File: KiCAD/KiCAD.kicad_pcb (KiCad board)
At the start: 2 copper layers, 200 x 150 mm, 199 parts, among them J1 Conn_01x02_Pin, J11 GRID_BIAS, J12 CATHODE_SENSE, J13 Conn_01x05, J14 Conn_01x02_Pin, J15 Conn_01x03_Pin, J16 Conn_01x05, J3 Conn_01x02_Pin, J4 8P8C_Shielded, J5 ENC_INT if needed, J6 TX/RX, J7 HV, J8 HV_INRUSH_BYPASS, J9 TR_SENSE, Q1 J310, Q2 2N7000, Q3 2N7000, Q4 2N7000, Q5 2N7000, Q6 2N7000, Q7 2N7000, T1 2N3906, T2 2N3906, U1 Si5351A_Breakout, U10 OPA454, U11 LM4040LP-5, U12 LM393, U13 OPA1641, U14 OPA1641, U15 LM7805_TO220, U16 AM26LS32ACN, U17 Adafruit_PCF8575_Breakout, U18 CD14538B, U19 L79L08_TO92, U20 ICL7660S, U3 MC1496, U4 MCP4921, U5 OPA454, U6 LM7171xIN, U7 LM7171xIN, U8 MCP4728, U9 LM7805_TO220

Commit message: kicad: L79L08 local decoupling; unlink bias sheet from root
- Add C17/C18 (0.33 uF Z5U SR205E334MAR) at L79L08 in/out to prevent
  oscillation and damp L7+U19 ringing
- New footprint xmitter:Kyocera_SR20_MLCC for the SR20 style radial MLCC
  (2.54 mm pitch, 5.08 x 3.175 mm body)
- Add SR-Series datasheet to Documentation/Components
- Unlink bias sheet from root schematic — first step in splitting the
  bias circuit onto its own PCB

Co-Authored-By: Claude Opus 4.7 <noreply@anthropic.com>
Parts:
- removed C19, C20, C23, C24, C27, C31: 100nF, Capacitor_THT:C_Disc_D5.0mm_W2.5mm_P5.00mm
- removed C21: 0.33uF, Capacitor_THT:C_Rect_L7.0mm_W3.5mm_P5.00mm
- removed C22: 0.1uF, Capacitor_THT:C_Disc_D5.0mm_W2.5mm_P5.00mm
- removed C25, C26, C30, C32, C33: 10uF, Capacitor_THT:CP_Radial_D5.0mm_P2.00mm
- removed C28, C29: 1nF, Capacitor_THT:C_Rect_L7.0mm_W3.5mm_P5.00mm
- removed D1, D2, D3, D4: 1N5817, Diode_THT:D_DO-41_SOD81_P10.16mm_Horizontal
- removed D5, D6: 1N4148, Diode_THT:D_DO-35_SOD27_P7.62mm_Horizontal
- removed J11: GRID_BIAS, Connector_PinHeader_2.54mm:PinHeader_1x02_P2.54mm_Vertical
- removed J12: CATHODE_SENSE, Connector_PinHeader_2.54mm:PinHeader_1x02_P2.54mm_Vertical
- removed J14, J3 (x2): Conn_01x02_Pin, Connector_PinHeader_2.54mm:PinHeader_1x02_P2.54mm_Vertical
- removed Q2, Q3: 2N7000, Package_TO_SOT_THT:TO-92_Inline
- removed R17: 27K, Resistor_THT:R_Axial_DIN0207_L6.3mm_D2.5mm_P10.16mm_Horizontal
- removed R18, R_GA1, R_GATE1, R_GB1: 10K, Resistor_THT:R_Axial_DIN0207_L6.3mm_D2.5mm_P10.16mm_Horizontal
- removed R19, R25: 4.7K, Resistor_THT:R_Axial_DIN0207_L6.3mm_D2.5mm_P10.16mm_Horizontal
- removed R20, R22: 7.5K, Resistor_THT:R_Axial_DIN0207_L6.3mm_D2.5mm_P10.16mm_Horizontal
- removed R21, R23: 470K, Resistor_THT:R_Axial_DIN0207_L6.3mm_D2.5mm_P10.16mm_Horizontal
- removed R24: 100K, Resistor_THT:R_Axial_DIN0207_L6.3mm_D2.5mm_P10.16mm_Horizontal
- removed RV1: 10K, Potentiometer_THT:Potentiometer_Bourns_3296W_Vertical
- removed R_FA1, R_FB1: 170K, Resistor_THT:R_Axial_DIN0207_L6.3mm_D2.5mm_P10.16mm_Horizontal
- removed R_GLA1, R_GLB1: 22K, Resistor_THT:R_Axial_DIN0207_L6.3mm_D2.5mm_P10.16mm_Horizontal
- removed R_PADA1, R_PADB1: 1K, Resistor_THT:R_Axial_DIN0207_L6.3mm_D2.5mm_P10.16mm_Horizontal
- removed R_Z1: 2.2K, Resistor_THT:R_Axial_DIN0207_L6.3mm_D2.5mm_P10.16mm_Horizontal
- removed TP10: CRASH_A, Connector_PinHeader_2.54mm:PinHeader_1x01_P2.54mm_Vertical
- removed TP8: GRID_CRASH, Connector_PinHeader_2.54mm:PinHeader_1x01_P2.54mm_Vertical
- removed TP9: CRASH_B, Connector_PinHeader_2.54mm:PinHeader_1x01_P2.54mm_Vertical
- removed U10, U5: OPA454, Package_DIP:DIP-8_W7.62mm
- removed U11: LM4040LP-5, Package_TO_SOT_THT:TO-92_Inline
- removed U12: LM393, Package_DIP:DIP-8_W7.62mm
- removed U13, U14: OPA1641, Package_DIP:DIP-8_W7.62mm
- removed U9: LM7805_TO220, Package_TO_SOT_THT:TO-220-3_Vertical
- C17, C18: value 1uF -> 0.33uF; footprint Capacitor_THT:C_Rect_L7.2mm_W4.5mm_P5.00mm -> xmitter:Kyocera_SR20_MLCC
- moved C17 259.5 mm to (93.8, 52.5)
- moved C18 255.0 mm to (87.8, 46.0)
- moved C48 21.8 mm to (99.5, 38.5)
- moved TP20 15.9 mm to (74.0, 42.0)
- moved J15 6.60 mm to (120.0, 158.5), turned to 180 degrees
- moved C43 3.53 mm to (95.5, 128.5)
- moved U19 3.35 mm to (95.0, 46.5)
- moved J6 2.54 mm to (120.5, 102.0)
- moved J7 2.54 mm to (120.5, 110.0)
- moved J8 2.54 mm to (120.5, 118.0)
- moved C42 2.50 mm to (96.0, 117.5)
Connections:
- C17 pad 1: +5V -> VEE
- C18 pad 1: GND -> Net-(U19-VI)
- C18 pad 2: -90V -> GND

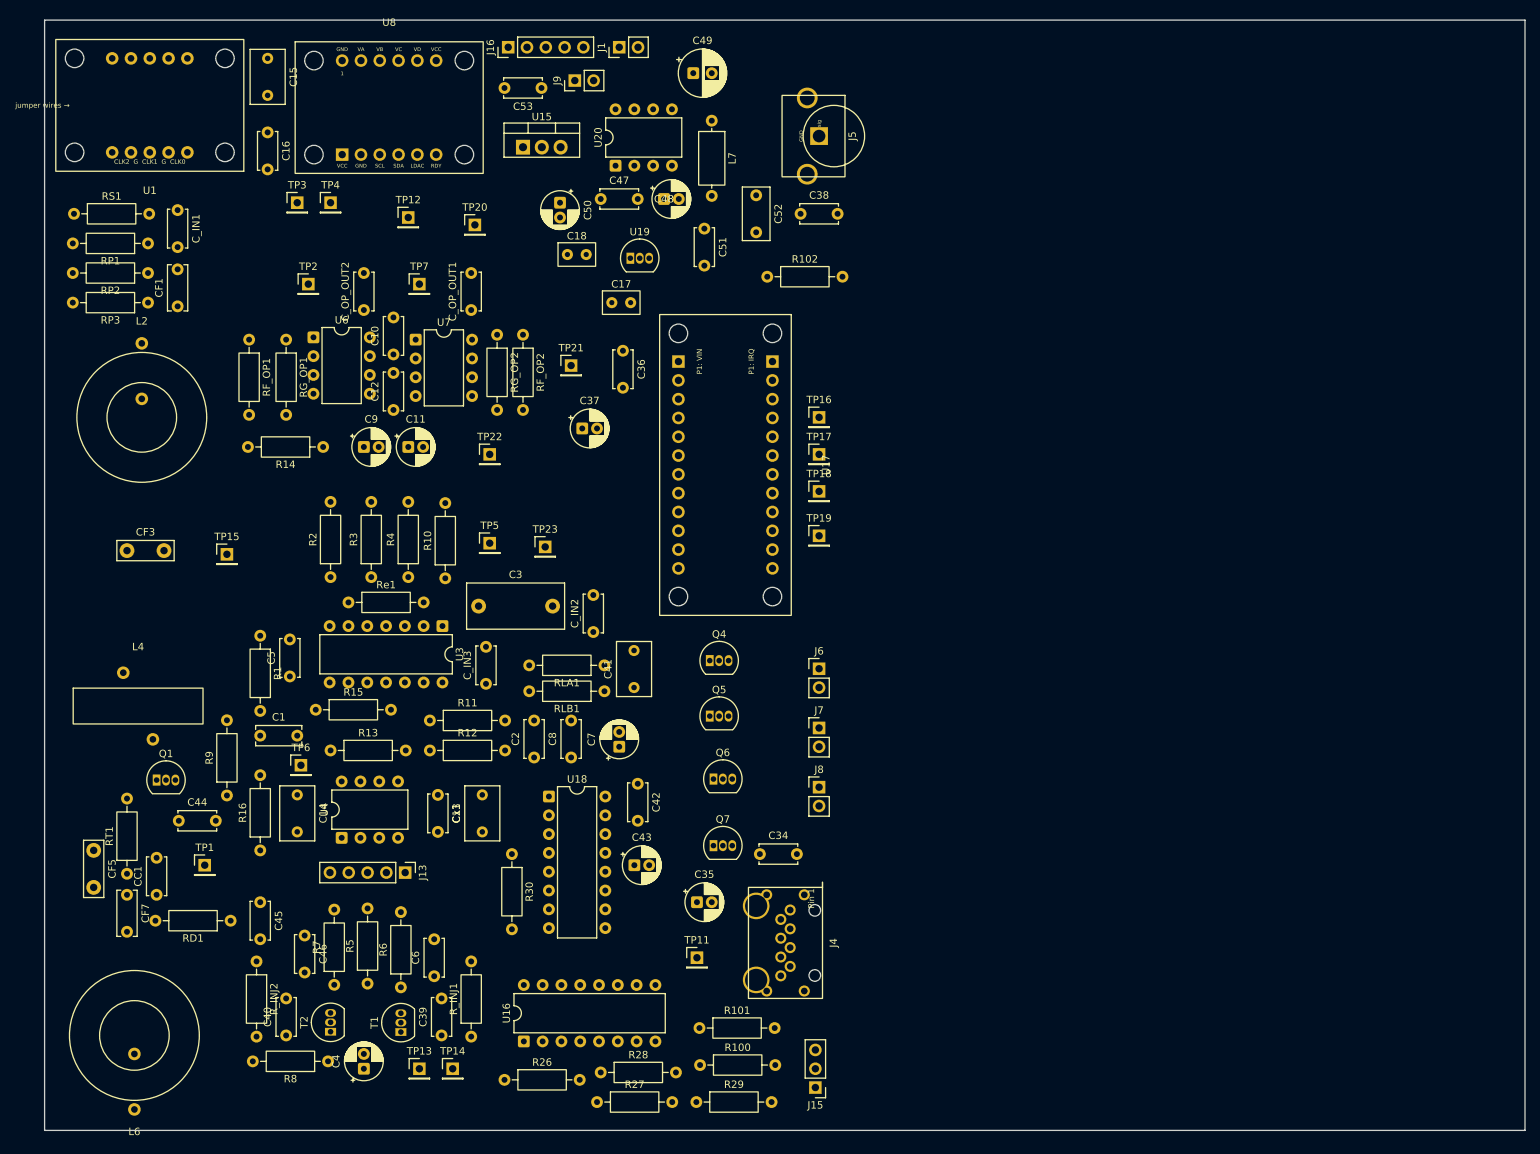
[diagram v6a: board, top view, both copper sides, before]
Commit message: kicad: net classes for Power/RF/HIZ with patterns for labeled nets
Adds Power (0.5mm/0.2mm), RF (0.4mm/0.25mm), and HIZ (0.3mm/0.25mm)
classes with color-coding. Patterns catch +12V/+5V/3V3/VEE/GND and
RAW_RF/MOD_RF_OUT+/- automatically. Anonymous nets (MC1496 out, DAC
output, T1/T2 collectors, injection paths) still need labels or
manual assignment.

Co-Authored-By: Claude Opus 4.7 <noreply@anthropic.com>
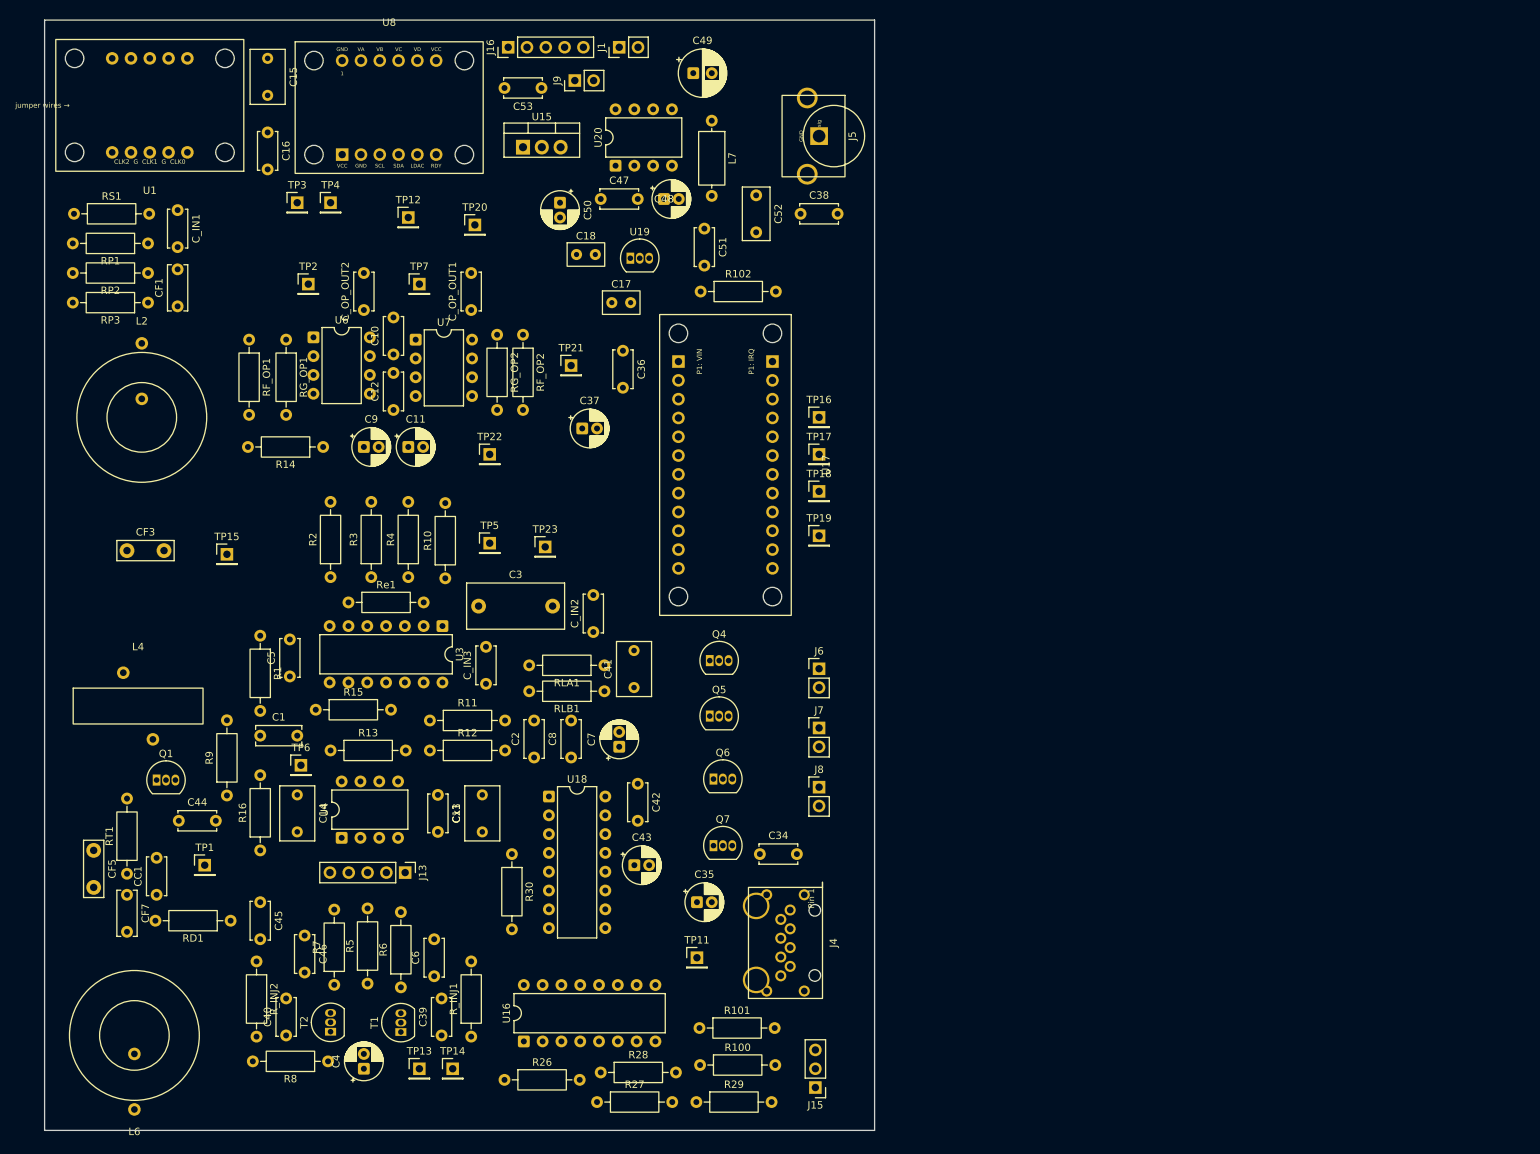
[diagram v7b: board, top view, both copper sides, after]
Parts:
- moved R102 9.22 mm to (104.5, 51.0)
- moved C18 1.23 mm to (89.0, 46.0)
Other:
- board size 200 x 150 mm -> 112.1 x 150 mm
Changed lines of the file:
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@@
 	(footprint "Resistor_THT:R_Axial_DIN0207_L6.3mm_D2.5mm_P10.16mm_Horizontal"
 		(layer "F.Cu")
-		(at 113.5 49)
+		(at 104.5 51)
 		(descr "Resistor, Axial_DIN0207 series, Axial, Horizontal, pin pitch=10.16mm, 0.25W = 1/4W, length*diameter=6.3*2.5mm^2, http://cdn-reichelt.de/documents/datenblatt/B400/1_4W%23YAG.pdf")
 		(tags "Resistor Axial_DIN0207 series Axial Horizontal pin pitch 10.16mm 0.25W = 1/4W length 6.3mm diameter 2.5mm")
@@
 	(footprint "xmitter:Kyocera_SR20_MLCC"
 		(layer "F.Cu")
-		(at 87.77 46)
+		(at 89 46)
 		(descr "Kyocera AVX SR20 radial multilayer ceramic capacitor, conformally coated (SkyCap SR-Series). Body 5.08 W x 3.175 T x 5.08 H mm max, lead spacing 2.54 mm, lead diameter 0.508 mm. Fits SR205E334MAR (0.33 uF Z5U 50 V) among others in the SR20 style.")
 		(tags "capacitor ceramic mlcc kyocera avx sr20 radial through-hole conformal")
@@
 	(gr_rect
 		(start 15.868452 14.329651)
-		(end 215.868452 164.329651)
+		(end 128 164.329651)
 		(stroke
 			(width 0.05)

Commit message: kicad: label critical anon nets on buffer_keyer for netclass matching
Global labels on MC1496 out (MC_OUT+/-), LM7171 driver outputs
(DRV_OUT+/-), T1/T2 collectors, and MCP4728 injection nodes
(VA_INJ/VB_INJ). Referenced by RF and HIZ patterns in netclass_patterns.

Co-Authored-By: Claude Opus 4.7 <noreply@anthropic.com>
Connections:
- net Net-(C_OP_OUT1-Pad1) renamed DRV_OUT-
- net Net-(C_OP_OUT2-Pad1) renamed DRV_OUT+
- net Net-(T1-C) renamed T1_COL
- net Net-(T2-C) renamed T2_COL
- net Net-(U3-OUT+) renamed MC_OUT+
- net Net-(U3-OUT-) renamed MC_OUT-
- net Net-(U8-VA) renamed VA_INJ
- net Net-(U8-VB) renamed VB_INJ
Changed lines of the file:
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@@
 			(layers "*.Cu" "*.Mask")
 			(remove_unused_layers no)
-			(net "Net-(U8-VB)")
+			(net "VB_INJ")
 			(pintype "passive")
 		)
@@
 			(layers "*.Cu" "*.Mask")
 			(remove_unused_layers no)
-			(net "Net-(C_OP_OUT2-Pad1)")
+			(net "DRV_OUT+")
 			(pintype "output")
 		)
@@
 			(layers "*.Cu" "*.Mask")
 			(remove_unused_layers no)
-			(net "Net-(U8-VA)")
+			(net "VA_INJ")
 			(pintype "passive")
 		)
@@
 			(layers "*.Cu" "*.Mask")
 			(remove_unused_layers no)
-			(net "Net-(T1-C)")
+			(net "T1_COL")
 			(pintype "passive")
 		)
@@
 			(layers "*.Cu" "*.Mask")
 			(remove_unused_layers no)
-			(net "Net-(C_OP_OUT1-Pad1)")
+			(net "DRV_OUT-")
 			(pintype "passive")
 		)
@@
 			(layers "*.Cu" "*.Mask")
 			(remove_unused_layers no)
-			(net "Net-(U3-OUT-)")
+			(net "MC_OUT-")
 			(pintype "passive")
 		)
@@
 			(layers "*.Cu" "*.Mask")
 			(remove_unused_layers no)
-			(net "Net-(U3-OUT+)")
+			(net "MC_OUT+")
 			(pinfunction "1_1")
 			(pintype "passive")
@@
 			(layers "*.Cu" "*.Mask")
 			(remove_unused_layers no)
-			(net "Net-(U8-VA)")
+			(net "VA_INJ")
 			(pinfunction "VA_7")
 			(pintype "output")
@@
 			(layers "*.Cu" "*.Mask")
 			(remove_unused_layers no)
-			(net "Net-(U8-VB)")
+			(net "VB_INJ")
 			(pinfunction "VB_8")
 			(pintype "output")
@@
 			(layers "*.Cu" "*.Mask")
 			(remove_unused_layers no)
-			(net "Net-(T2-C)")
+			(net "T2_COL")
 			(pintype "passive")
 		)
@@
 			(layers "*.Cu" "*.Mask")
 			(remove_unused_layers no)
-			(net "Net-(U3-OUT-)")
+			(net "MC_OUT-")
 			(pinfunction "1_1")
 			(pintype "passive")
@@
 			(layers "*.Cu" "*.Mask")
 			(remove_unused_layers no)
-			(net "Net-(T1-C)")
+			(net "T1_COL")
 			(pintype "passive")
 		)
@@
 			(layers "*.Cu" "*.Mask")
 			(remove_unused_layers no)
-			(net "Net-(T1-C)")
+			(net "T1_COL")
 			(pinfunction "1_1")
 			(pintype "passive")
@@
 			(layers "*.Cu" "*.Mask")
 			(remove_unused_layers no)
-			(net "Net-(T2-C)")
+			(net "T2_COL")
 			(pinfunction "1_1")
 			(pintype "passive")
@@
 			(layers "*.Cu" "*.Mask")
 			(remove_unused_layers no)
-			(net "Net-(T1-C)")
+			(net "T1_COL")
 			(pinfunction "C_3")
 			(pintype "passive")
@@
 			(layers "*.Cu" "*.Mask")
 			(remove_unused_layers no)
-			(net "Net-(C_OP_OUT2-Pad1)")
+			(net "DRV_OUT+")
 			(pintype "passive")
 		)
@@
 			(layers "*.Cu" "*.Mask")
 			(remove_unused_layers no)
-			(net "Net-(U3-OUT+)")
+			(net "MC_OUT+")
 			(pintype "passive")
 		)
@@
 			(layers "*.Cu" "*.Mask")
 			(remove_unused_layers no)
-			(net "Net-(U3-OUT-)")
+			(net "MC_OUT-")
 			(pintype "passive")
 		)
@@
 			(layers "*.Cu" "*.Mask")
 			(remove_unused_layers no)
-			(net "Net-(T2-C)")
+			(net "T2_COL")
 			(pintype "passive")
 		)
@@
 			(layers "*.Cu" "*.Mask")
 			(remove_unused_layers no)
-			(net "Net-(U3-OUT+)")
+			(net "MC_OUT+")
 			(pintype "passive")
 		)
@@
 			(layers "*.Cu" "*.Mask")
 			(remove_unused_layers no)
-			(net "Net-(C_OP_OUT1-Pad1)")
+			(net "DRV_OUT-")
 			(pintype "output")
 		)
@@
 			(layers "*.Cu" "*.Mask")
 			(remove_unused_layers no)
-			(net "Net-(C_OP_OUT2-Pad1)")
+			(net "DRV_OUT+")
 			(pintype "passive")
 		)
@@
 			(layers "*.Cu" "*.Mask")
 			(remove_unused_layers no)
-			(net "Net-(C_OP_OUT1-Pad1)")
+			(net "DRV_OUT-")
 			(pintype "passive")
 		)
@@
 			(layers "*.Cu" "*.Mask")
 			(remove_unused_layers no)
-			(net "Net-(T2-C)")
+			(net "T2_COL")
 			(pinfunction "C_3")
 			(pintype "passive")
@@
 			(layers "*.Cu" "*.Mask")
 			(remove_unused_layers no)
-			(net "Net-(U3-OUT+)")
+			(net "MC_OUT+")
 			(pinfunction "OUT+_6")
 			(pintype "passive")
@@
 			(layers "*.Cu" "*.Mask")
 			(remove_unused_layers no)
-			(net "Net-(U3-OUT-)")
+			(net "MC_OUT-")
 			(pinfunction "OUT-_12")
 			(pintype "passive")
